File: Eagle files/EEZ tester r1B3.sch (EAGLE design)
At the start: 84 parts, among them IC1 LM358, IC2 LM5574MTX/NOPB, K1 RT314005, Q1 2N7002, Q2 2N7002, Q3 2N7002, Q4 2N7002, Q5 2N7002, Q6 2N7002, SW1 1301.9316, SW2 1301.9316, X1 39303035, X2 282836-3, X3 SSW-113-02-S-D-RA, X4 282836-5, X5 282836-3, X6 09185166324

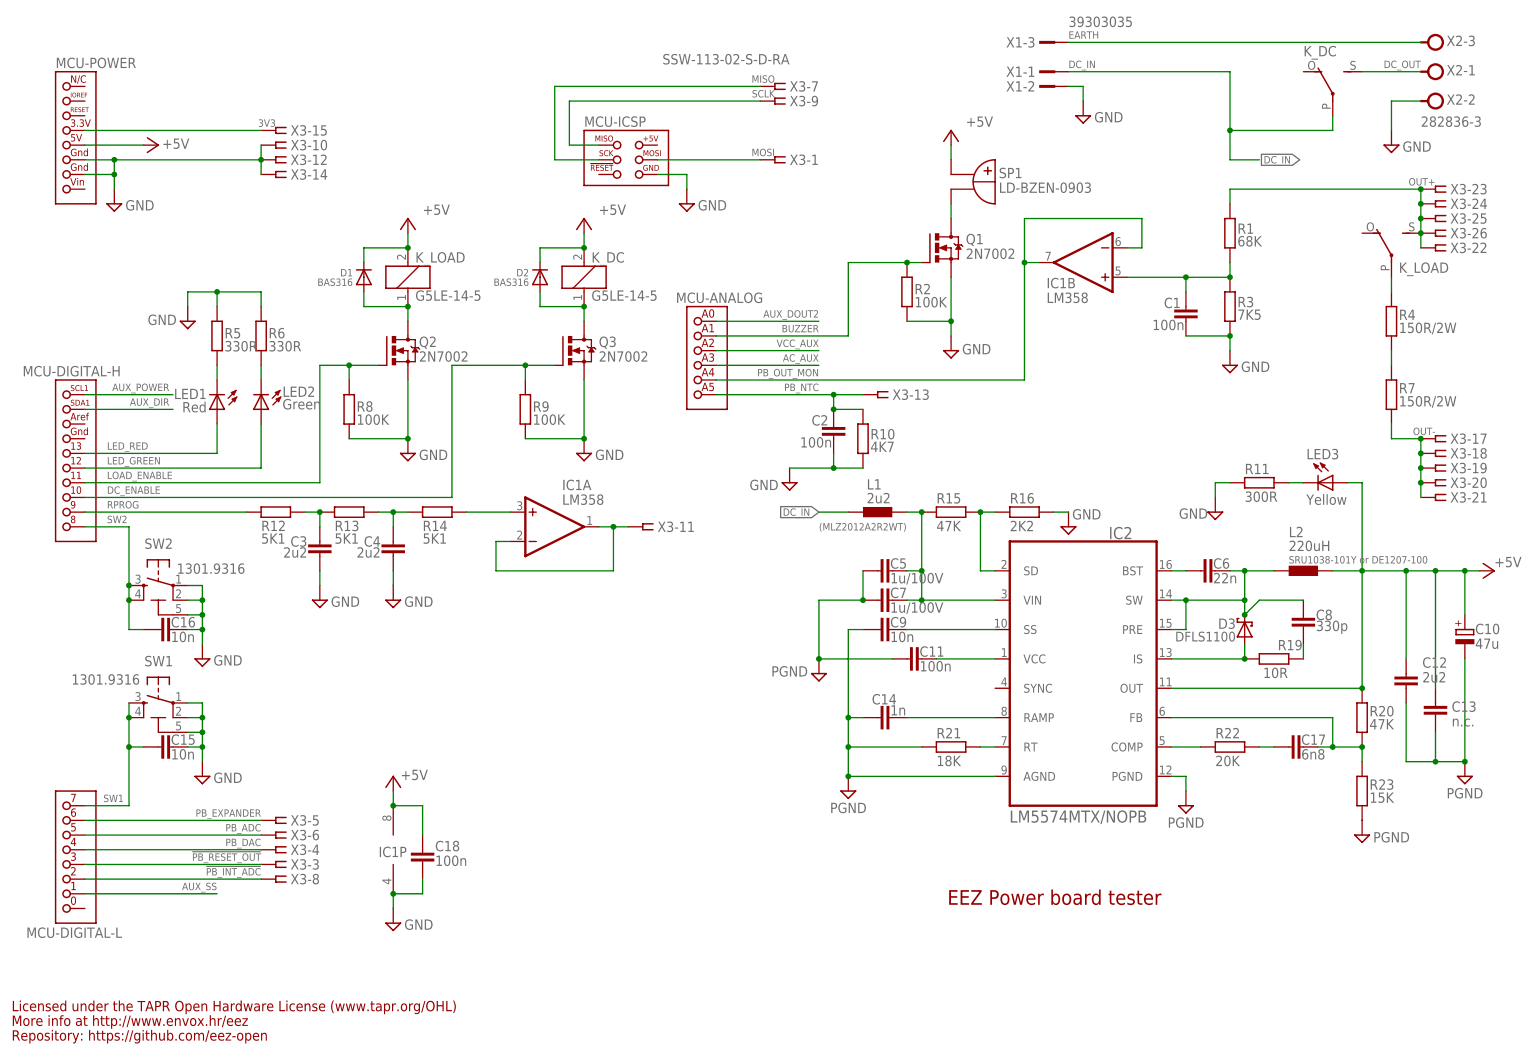
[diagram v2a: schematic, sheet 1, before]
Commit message: pinout redefinition
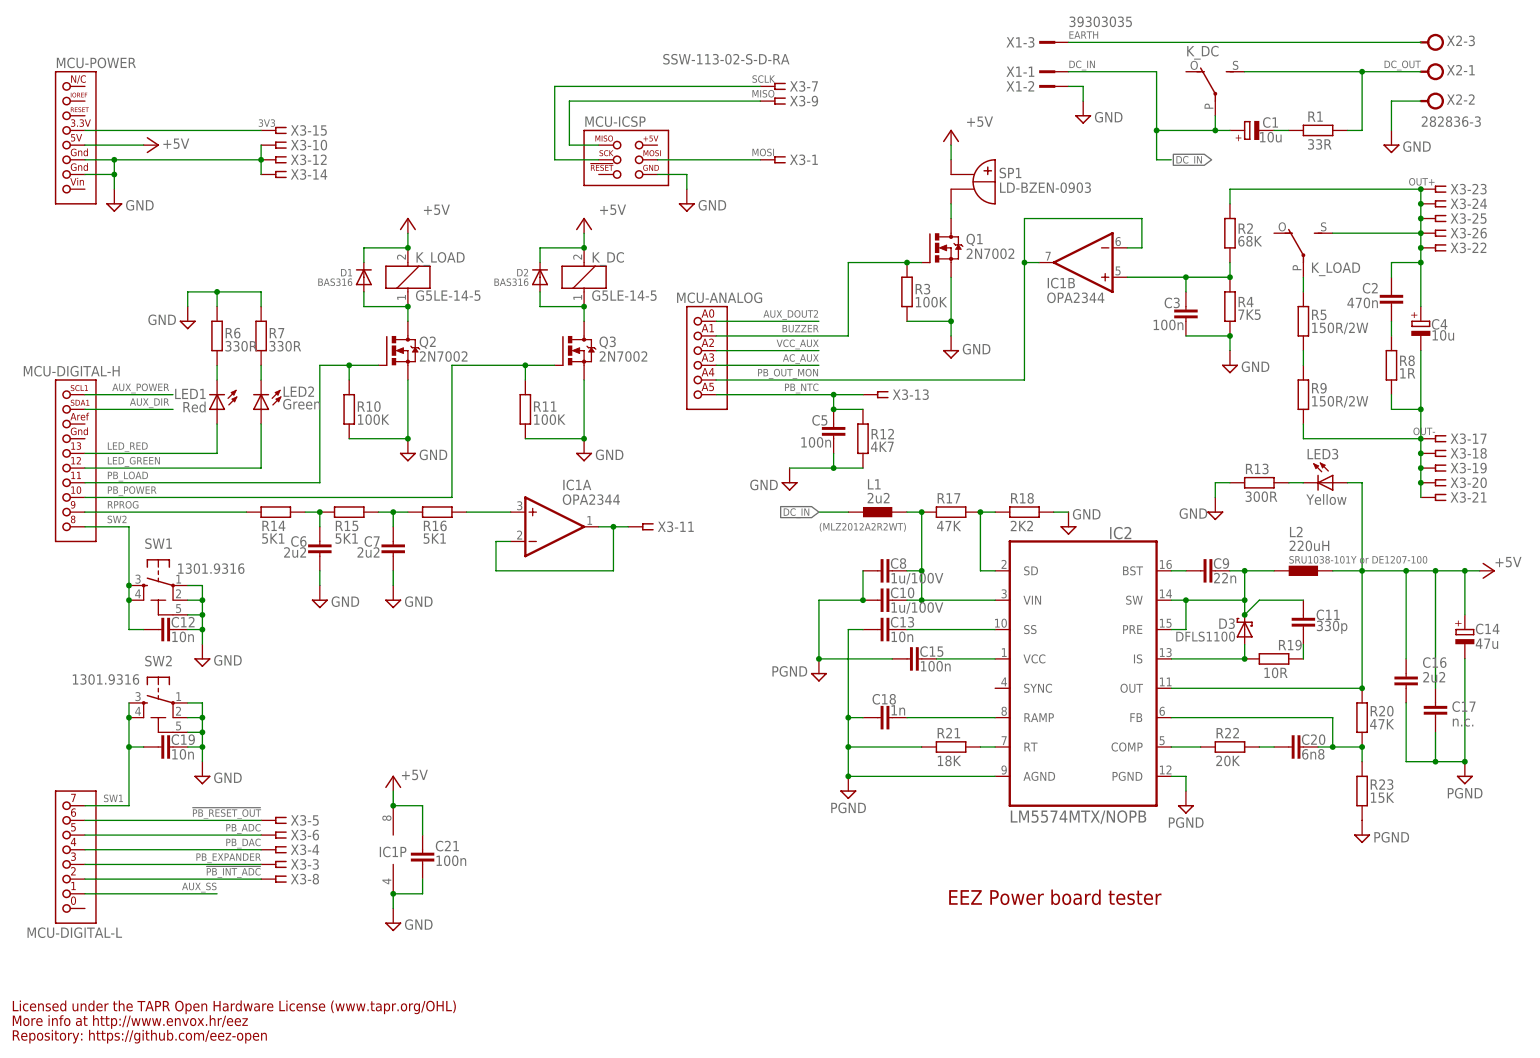
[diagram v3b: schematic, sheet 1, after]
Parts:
- added C21: 100n, rcl:C-EUC0603
- added C22: 220n, rcl:C-EU150-084X183
- added C23: 220u, EEZ_Lib1:ECAPPANASONIC_H
- added R17: 47K, rcl:R-EU_R0805
- added R18: 2K2, rcl:R-EU_R0805
- C1: value 100n -> 10u; device rcl:C-EUC0603 -> MyLib6:ECAPPANASONIC_C
- C10: value 47u -> 1u/100V; device EEZ_Lib1:ECAPPANASONIC_H -> rcl:C-EUC1206
- C11: value 100n -> 330p; device rcl:C-EUC0603 -> rcl:C-EUC0805
- C12: value 2u2 -> 10n
- C13: value n.c. -> 10n
- C14: value 1n -> 47u; device rcl:C-EUC0805 -> EEZ_Lib1:ECAPPANASONIC_H
- C15: value 10n -> 100n; device rcl:C-EUC0805 -> rcl:C-EUC0603
- C16: value 10n -> 2u2
- C17: value 6n8 -> n.c.
- C18: value 100n -> 1n; device rcl:C-EUC0603 -> rcl:C-EUC0805
- C19: value 220n -> 10n; device rcl:C-EU150-084X183 -> rcl:C-EUC0805
- C2: value 100n -> 470n; device rcl:C-EUC0603 -> rcl:C-EUC0805
- C20: value 220u -> 6n8; device EEZ_Lib1:ECAPPANASONIC_H -> rcl:C-EUC0805
- C3: value 2u2 -> 100n; device rcl:C-EUC0805 -> rcl:C-EUC0603
- C4: value 2u2 -> 10u; device rcl:C-EUC0805 -> MyLib6:ECAPPANASONIC_C
- C5: value 1u/100V -> 100n; device rcl:C-EUC1206 -> rcl:C-EUC0603
- C6: value 22n -> 2u2
- C7: value 1u/100V -> 2u2; device rcl:C-EUC1206 -> rcl:C-EUC0805
- C8: value 330p -> 1u/100V; device rcl:C-EUC0805 -> rcl:C-EUC1206
- C9: value 10n -> 22n
- IC1: value LM358 -> OPA2344
- R1: value 68K -> 33R
- R10: value 4K7 -> 100K
- R11, R26: value 300R -> 100K
- R12: value 5K1 -> 4K7
- R13: value 5K1 -> 300R
- R15: value 47K -> 5K1
- R16: value 2K2 -> 5K1
- R2: value 100K -> 68K
- R25: value 2K2 -> 100K
- R27: value 330R/2W -> 2K2; device rcl:R-EU_R2512 -> rcl:R-EU_R0805
- R28: value 1M -> 2K2
- R29: value 100K -> 200R
- R3: value 7K5 -> 100K
- R30: value 100K -> 330R/2W; device rcl:R-EU_R0805 -> rcl:R-EU_R2512
- R33: value 2K2 -> 1M
- R4: value 150R/2W -> 7K5; device rcl:R-EU_0617/22 -> rcl:R-EU_R0805
- R5: value 330R -> 150R/2W; device rcl:R-EU_R0805 -> rcl:R-EU_0617/22
- R7: value 150R/2W -> 330R; device rcl:R-EU_0617/22 -> rcl:R-EU_R0805
- R8: value 100K -> 1R
- R9: value 100K -> 150R/2W; device rcl:R-EU_R0805 -> rcl:R-EU_0617/22
- renumbered R34 to R32, R35 to R31, ZD2 to ZD1
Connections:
- removed net DC_ENABLE: MCU-DIGITAL-H.10, Q3.G, R9.2
- removed net LOAD_ENABLE: MCU-DIGITAL-H.11, Q2.G, R8.2
- new net N$5: C1.-, R1.1
- new net N$94: C2.2, R8.2
- new net PB_LOAD: MCU-DIGITAL-H.11, Q2.G, R10.2
- new net PB_POWER: MCU-DIGITAL-H.10, Q3.G, R11.2
- net !PB_RESET_OUT: now also MCU-DIGITAL-L.6(PH3), X3-5.1; no longer MCU-DIGITAL-L.3(PE5), X3-3.1
- net +5V: now also C14.+, C16.1, C17.1, C21.1, R28.2; no longer C10.+, C12.1, C13.1, C18.1, R25.2
- net AC_AUX: now also R28.1; no longer R25.1
- net AUX_DIR: now also R25.2; no longer R29.2
- net AUX_SS: now also R26.2; no longer R30.2
- net BUZZER: now also R3.2; no longer R2.2
- net DC_IN: now also C1.+
- net DC_OUT: now also R1.2
- net DC_PREG1: now also C10.1, C8.1, R17.2; no longer C5.1, C7.1, R15.2
- net GND: now also C10.2, C14.-, C15.1, C17.2, C18.1, C19.2, C21.2, C3.1, C5.1, C6.2, C8.2, R10.1, R12.2, R13.1, R18.1, R25.1, R26.1, R3.1, R4.2, R7.2; no longer C1.1, C10.-, C11.1, C14.1, C15.2, C18.2, C2.1, C3.2, C4.2, C5.2, C9.2, R10.2, R16.1, R2.1, R29.1, R3.2, R30.1, R5.2, R8.1, R9.1
- net MISO: now also MCU-ICSP.MISO, X3-9.1; no longer MCU-ICSP.SCK, X3-7.1
- net N$1: now also R5.1, R9.2; no longer R4.1, R7.2
- net N$128: now also C20.1; no longer C17.1
- net N$13: now also C6.1, R14.1, R15.2; no longer C3.1, R12.1, R13.2
- net N$131: now also C9.2; no longer C6.2
- net N$15: now also R6.1; no longer R5.1
- net N$16: now also R7.1; no longer R6.1
- net N$166: now also C15.2; no longer C11.2
- net N$167: now also C18.2; no longer C14.2
- net N$168: now also C13.1; no longer C9.1
- net N$180: now also R17.1, R18.2; no longer R15.1, R16.2
- net N$2: now also R5.2; no longer R4.2
- net N$227: now also R16.1; no longer R14.1
- net N$27: now also R30.1; no longer R27.1
- net N$28: now also C22.2, R30.2, R33.1; no longer C19.2, R27.2, R28.1
- net N$29: now also C22.1, R33.2; no longer C19.1, R28.2
- net N$3: now also R13.2; no longer R11.2
- net N$31: now also C23.-; no longer C20.-
- net N$33: now also R29.2; no longer R26.2
- net N$34: now also C23.+, R29.1; no longer C20.+, R26.1
- net N$37: now also R27.2; no longer R33.2
- net N$46: now also C11.2; no longer C8.2
- net N$7: now also C3.2, R2.2, R4.1; no longer C1.2, R1.2, R3.1
- net N$77: now also C20.2; no longer C17.2
- net N$9: now also C7.1, R15.1, R16.2; no longer C4.1, R13.1, R14.2
- net OUT+: now also C2.1, C4.+, R2.1; no longer R1.1
- net OUT-: now also C4.-, R8.1, R9.1; no longer R7.1
- net PB_EXPANDER: now also MCU-DIGITAL-L.3(PE5), X3-3.1; no longer MCU-DIGITAL-L.6(PH3), X3-5.1
- net PB_NTC: now also C5.2, R12.1; no longer C2.2, R10.1
- net RPROG: now also R14.2; no longer R12.2
- net SCLK: now also MCU-ICSP.SCK, X3-7.1; no longer MCU-ICSP.MISO, X3-9.1
- net SW: now also C11.1, C9.1; no longer C6.1, C8.1
- net SW1: now also C19.1, SW2.3, SW2.4; no longer C15.1, SW1.3, SW1.4
- net SW2: now also C12.1, SW1.3, SW1.4; no longer C16.1, SW2.3, SW2.4
- net VCC_AUX: now also R27.1; no longer R33.1
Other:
- moved on the sheet: C11, C12, C13, C15, C16, C17, C18, C2, C3, C5, C6, C7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
